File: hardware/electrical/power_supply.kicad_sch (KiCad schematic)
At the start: 25 parts, among them J1 USB_OTG, J3 Conn_01x02_Male, Q1 IRLZ34N, Q2 IRLZ34N, Q3 IRLML5203, Q4 IRLML5203, SW1 SW_DIP_x01, U1 MCP73831-2-OT, U2 AP9101CK6, U3 MCP1700-3302E_SOT23

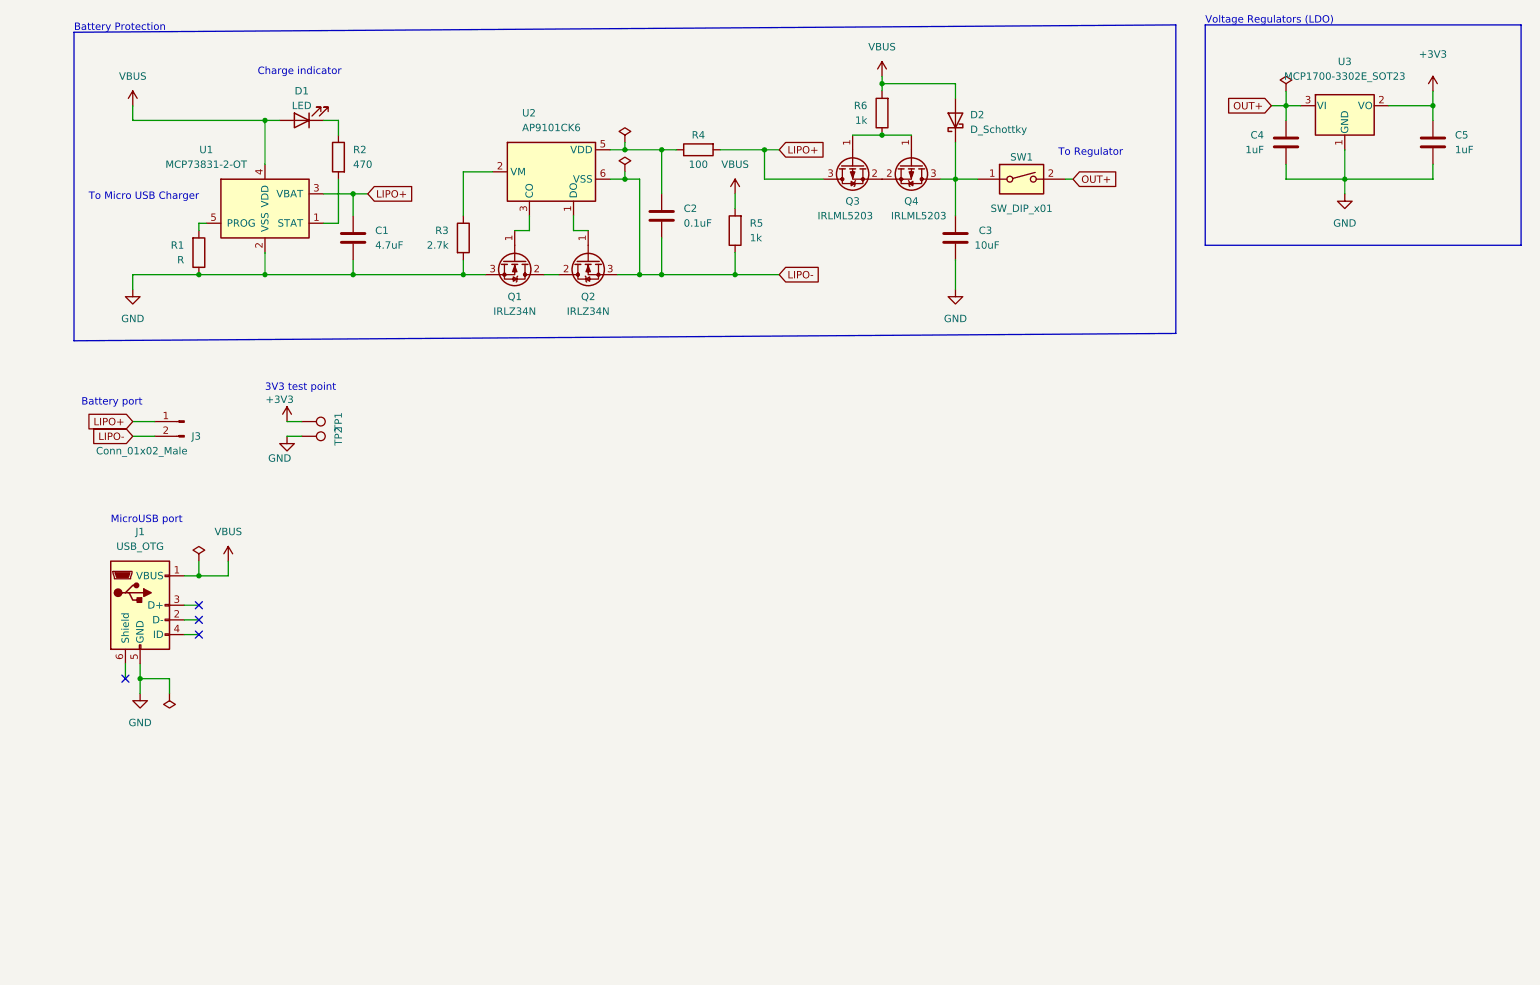
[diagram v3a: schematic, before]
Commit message: Mark R1 as TBD and add value to J3
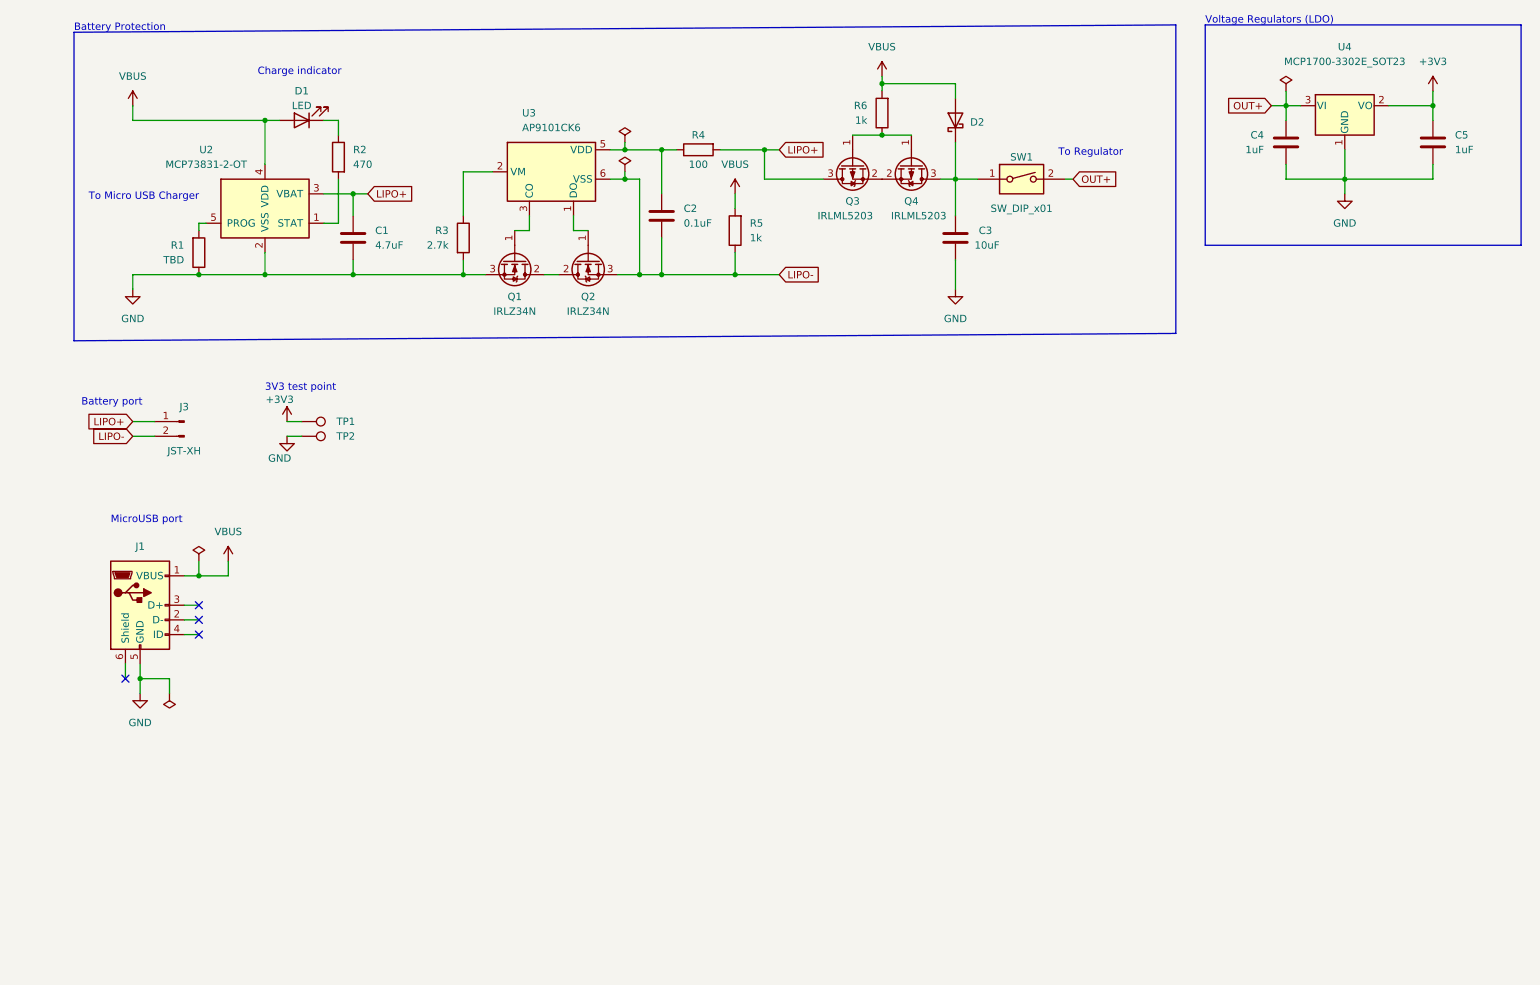
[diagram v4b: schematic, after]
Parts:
- J1: value USB_OTG -> Micro USB B
- J3: value Conn_01x02_Male -> JST-XH
- R1: value R -> TBD
- renumbered U1 to U2, U2 to U3, U3 to U4
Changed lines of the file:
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@@
   (symbol (lib_id "Connector:USB_OTG") (at 39.37 124.46 0) (unit 1)
     (in_bom yes) (on_board yes) (fields_autoplaced)
-    (property "Reference" "J1" (id 0) (at 39.37 111.76 0))
-    (property "Value" "USB_OTG" (id 1) (at 39.37 114.3 0))
+    (property "Reference" "J1" (id 0) (at 39.37 114.3 0))
+    (property "Value" "Micro USB B" (id 1) (at 39.37 114.3 0)
+      (effects (font (size 1.27 1.27)) hide)
+    )
     (property "Footprint" "Connector_USB:USB_Micro-B_GCT_USB3076-30-A" (id 2) (at 43.18 125.73 0)
       (effects (font (size 1.27 1.27)) hide)
@@
   (symbol (lib_id "Connector:TestPoint") (at 67.31 95.25 270) (unit 1)
     (in_bom yes) (on_board yes)
-    (property "Reference" "TP2" (id 0) (at 73.66 95.25 0))
+    (property "Reference" "TP2" (id 0) (at 74.93 95.25 90))
     (property "Value" "TestPoint" (id 1) (at 69.3421 97.79 0)
       (effects (font (size 1.27 1.27)) (justify left) hide)
@@
   (symbol (lib_id "power:PWR_FLAG") (at 237.49 35.56 0) (unit 1)
     (in_bom yes) (on_board yes)
-    (property "Reference" "#FLG?" (id 0) (at 237.49 33.655 0)
+    (property "Reference" "#FLG01" (id 0) (at 237.49 33.655 0)
       (effects (font (size 1.27 1.27)) hide)
     )
@@
       (effects (font (size 1.27 1.27)) (justify right))
     )
-    (property "Value" "R" (id 1) (at 46.99 64.77 0)
+    (property "Value" "TBD" (id 1) (at 46.99 64.77 0)
       (effects (font (size 1.27 1.27)) (justify right))
     )
@@
       (effects (font (size 1.27 1.27)) hide)
     )
-    (property "Value" "+3V3" (id 1) (at 262.89 29.21 0))
+    (property "Value" "+3V3" (id 1) (at 262.89 30.48 0))
     (property "Footprint" "" (id 2) (at 262.89 35.56 0)
       (effects (font (size 1.27 1.27)) hide)
@@
   (symbol (lib_id "Connector:TestPoint") (at 67.31 92.71 270) (unit 1)
     (in_bom yes) (on_board yes)
-    (property "Reference" "TP1" (id 0) (at 73.66 92.71 0))
+    (property "Reference" "TP1" (id 0) (at 74.93 92.71 90))
     (property "Value" "TestPoint" (id 1) (at 69.3421 95.25 0)
       (effects (font (size 1.27 1.27)) (justify left) hide)
@@
   (symbol (lib_id "Battery_Management:MCP73831-2-OT") (at 60.96 55.88 0) (unit 1)
     (in_bom yes) (on_board yes)
-    (property "Reference" "U1" (id 0) (at 50.8 45.72 0))
+    (property "Reference" "U2" (id 0) (at 50.8 45.72 0))
     (property "Value" "MCP73831-2-OT" (id 1) (at 50.8 48.26 0))
     (property "Footprint" "Package_TO_SOT_SMD:SOT-23-5" (id 2) (at 62.23 62.23 0)
@@
   (symbol (lib_id "Battery_Management:AP9101CK6") (at 110.49 49.53 0) (unit 1)
     (in_bom yes) (on_board yes)
-    (property "Reference" "U2" (id 0) (at 105.41 39.37 0)
+    (property "Reference" "U3" (id 0) (at 105.41 39.37 0)
       (effects (font (size 1.27 1.27)) (justify left))
     )
@@
   (symbol (lib_id "Connector:Conn_01x02_Male") (at 46.99 92.71 0) (mirror y) (unit 1)
     (in_bom yes) (on_board yes)
-    (property "Reference" "J3" (id 0) (at 48.26 95.2501 0)
-      (effects (font (size 1.27 1.27)) (justify right))
-    )
-    (property "Value" "Conn_01x02_Male" (id 1) (at 31.75 97.79 0)
-      (effects (font (size 1.27 1.27)) (justify right))
-    )
+    (property "Reference" "J3" (id 0) (at 46.99 90.17 0))
+    (property "Value" "JST-XH" (id 1) (at 46.99 97.79 0))
     (property "Footprint" "Connector_PinHeader_2.00mm:PinHeader_1x02_P2.00mm_Vertical" (id 2) (at 46.99 92.71 0)
       (effects (font (size 1.27 1.27)) hide)
@@
   )
   (symbol (lib_id "Regulator_Linear:MCP1700-3302E_SOT23") (at 247.65 38.1 0) (unit 1)
-    (in_bom yes) (on_board yes) (fields_autoplaced)
-    (property "Reference" "U3" (id 0) (at 247.65 30.48 0))
-    (property "Value" "MCP1700-3302E_SOT23" (id 1) (at 247.65 33.02 0))
+    (in_bom yes) (on_board yes)
+    (property "Reference" "U4" (id 0) (at 247.65 27.94 0))
+    (property "Value" "MCP1700-3302E_SOT23" (id 1) (at 247.65 30.48 0))
     (property "Footprint" "Package_TO_SOT_SMD:SOT-23" (id 2) (at 247.65 32.385 0)
       (effects (font (size 1.27 1.27)) hide)
@@
   (symbol (lib_id "power:+3V3") (at 64.77 92.71 0) (unit 1)
     (in_bom yes) (on_board yes)
-    (property "Reference" "#PWR?" (id 0) (at 64.77 96.52 0)
+    (property "Reference" "#PWR034" (id 0) (at 64.77 96.52 0)
       (effects (font (size 1.27 1.27)) hide)
     )
@@
   (symbol (lib_id "Device:D_Schottky") (at 180.34 40.64 90) (unit 1)
     (in_bom yes) (on_board yes) (fields_autoplaced)
-    (property "Reference" "D2" (id 0) (at 182.88 39.6874 90)
+    (property "Reference" "D2" (id 0) (at 182.88 40.9574 90)
       (effects (font (size 1.27 1.27)) (justify right))
     )
     (property "Value" "D_Schottky" (id 1) (at 182.88 42.2274 90)
-      (effects (font (size 1.27 1.27)) (justify right))
+      (effects (font (size 1.27 1.27)) (justify right) hide)
     )
     (property "Footprint" "Diode_THT:D_DO-41_SOD81_P2.54mm_Vertical_AnodeUp" (id 2) (at 180.34 40.64 0)
@@
   (symbol (lib_id "power:GND") (at 64.77 95.25 0) (unit 1)
     (in_bom yes) (on_board yes)
-    (property "Reference" "#PWR?" (id 0) (at 64.77 101.6 0)
-      (effects (font (size 1.27 1.27)) hide)
-    )
+    (property "Reference" "#PWR035" (id 0) (at 64.77 101.6 0)
+      (effects (font (size 1.27 1.27)) hide)
+    )

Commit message: Remove SW1 and D1
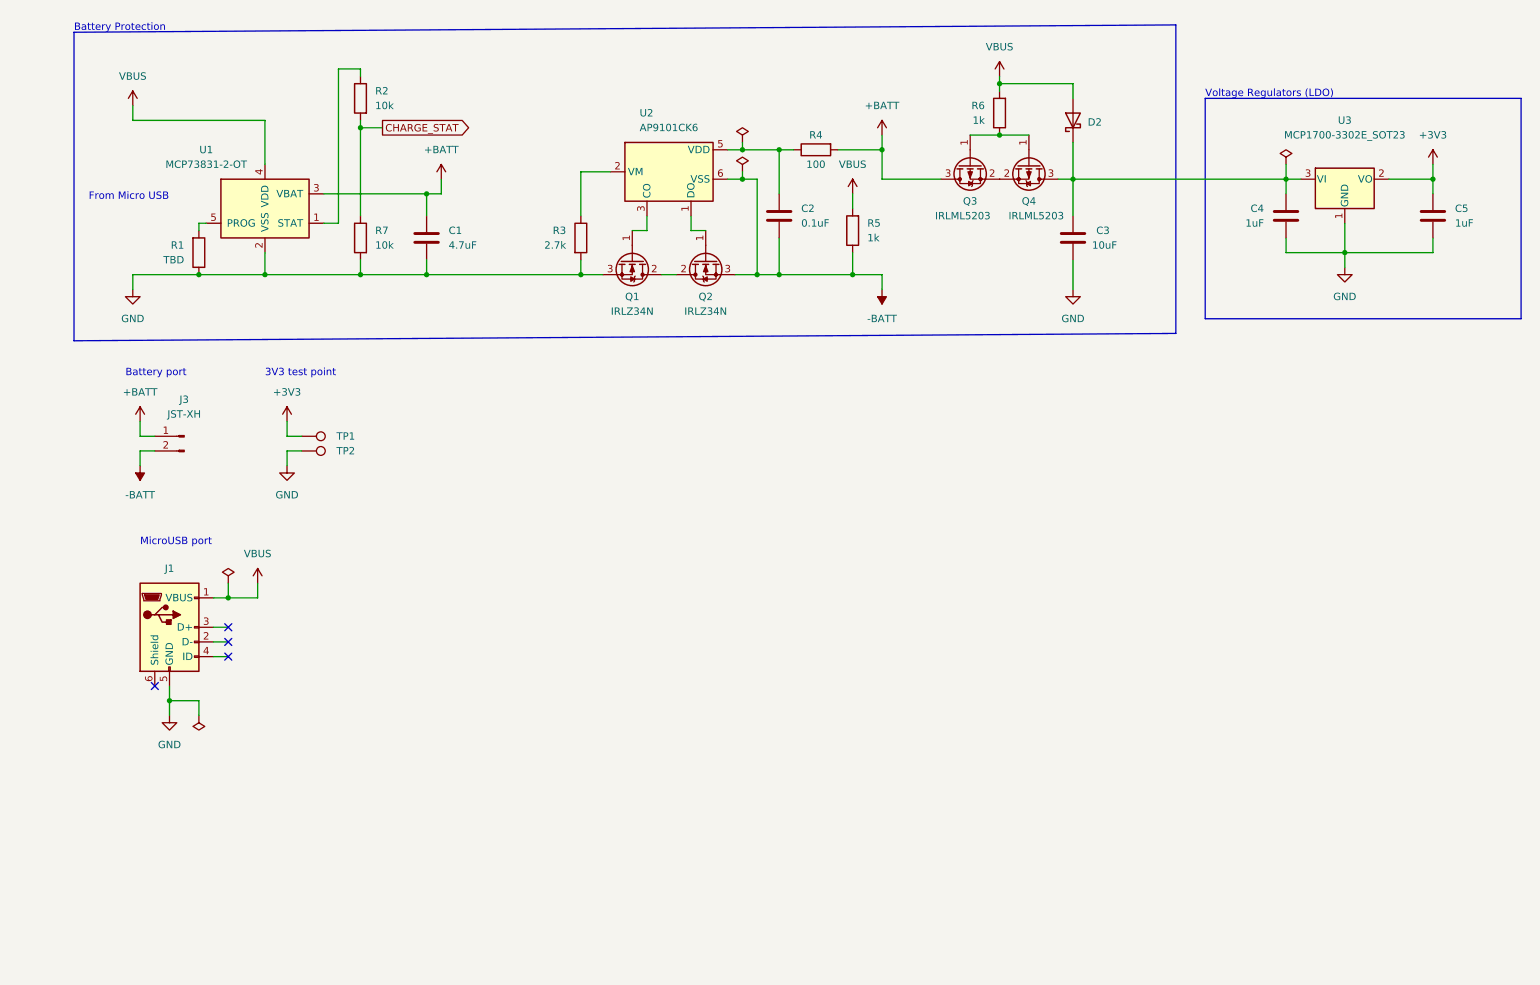
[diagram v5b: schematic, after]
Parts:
- removed D1: LED, LED_SMD:LED_1206_3216Metric, symbol Device:LED
- removed SW1: SW_DIP_x01, Connector_PinHeader_2.00mm:PinHeader_1x02_P2.00mm_Vertical, symbol Switch:SW_DIP_x01
- added R7: 10k, Resistor_SMD:R_0805_2012Metric_Pad1.20x1.40mm_HandSolder, symbol Device:R
- R2: value 470 -> 10k
- renumbered U2 to U1, U3 to U2, U4 to U3
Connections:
- net OUT+ is gone; now on an unnamed net: C4.2, U3.3 (VI)
- net GND: now also R7.2
- net at U1.1 (STAT): now also R2.1; no longer R2.2
- net LIPO+ renamed +BATT
- net LIPO- renamed -BATT
- new net CHARGE_STAT: R2.2, R7.1
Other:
- note added: "From Micro USB"
- note removed: "Charge indicator"
- note removed: "To Micro USB Charger"
- note removed: "To Regulator"
- moved on the sheet: C1, C2, C3, C4, C5, D2, J3, Q1, Q2, Q3, Q4, R2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

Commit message: Add USB VBUS filtering
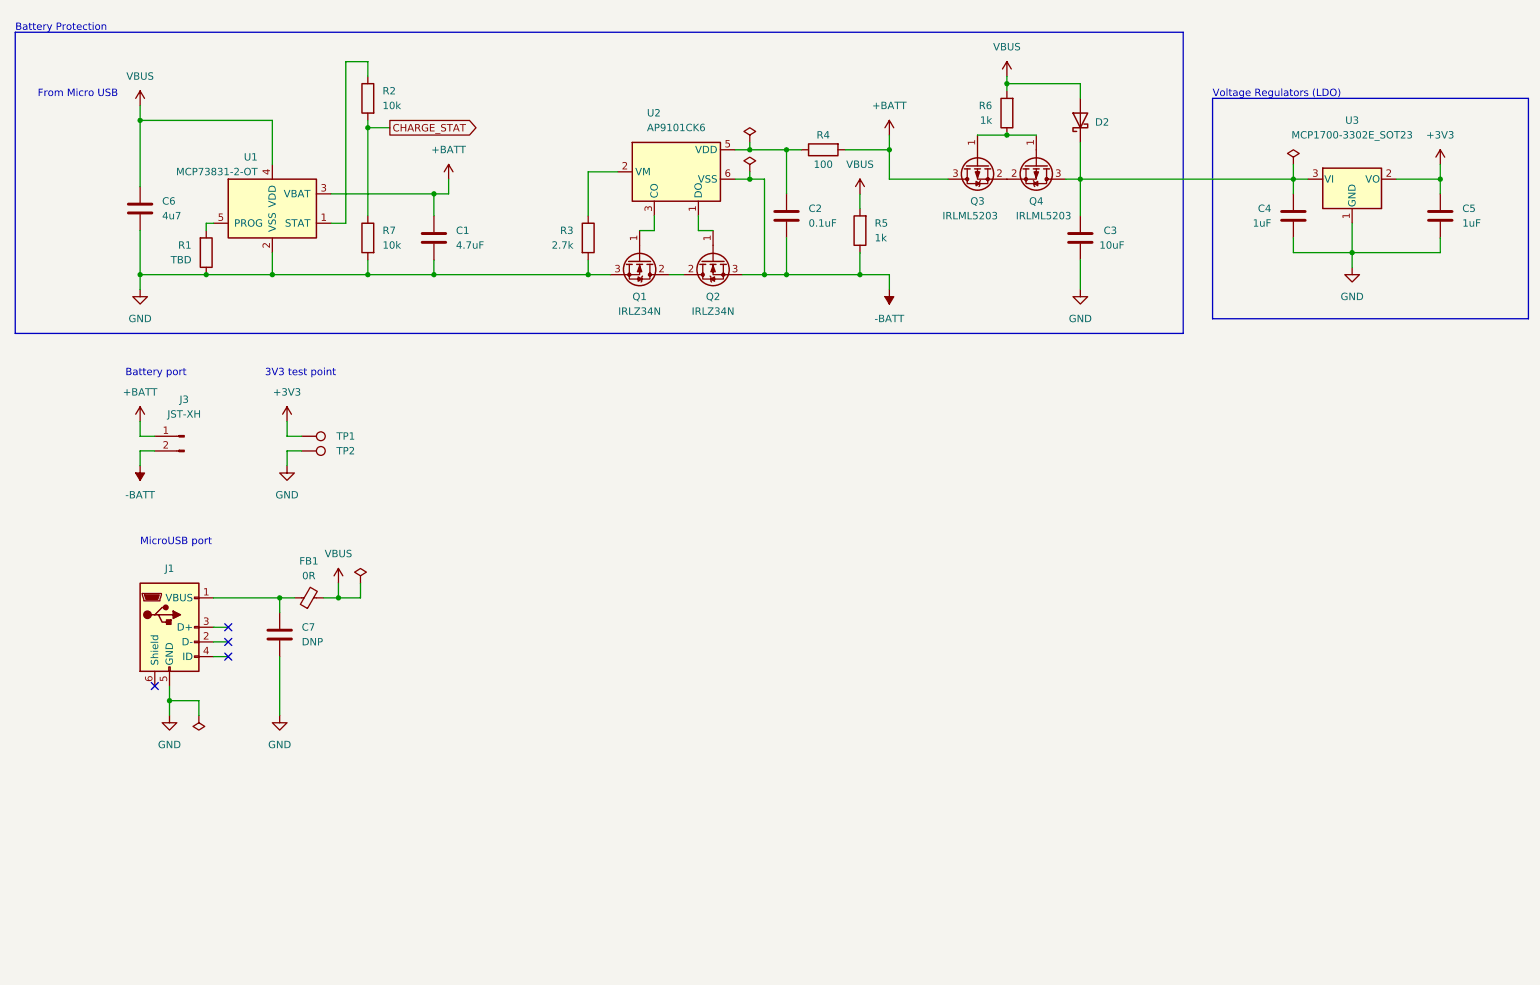
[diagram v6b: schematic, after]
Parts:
- added C6: 4u7, symbol Device:C
- added C7: DNP, symbol Device:C
- added FB1: 0R, symbol Device:FerriteBead_Small
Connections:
- net GND: now also C6.2, C7.2
- net VBUS: now also C6.1, FB1.2; no longer J1.1 (VBUS)
- new net: C7.1, FB1.1, J1.1 (VBUS)
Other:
- moved on the sheet: C1, C2, C3, C4, C5, D2, Q1, Q2, Q3, Q4, R1, R2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
